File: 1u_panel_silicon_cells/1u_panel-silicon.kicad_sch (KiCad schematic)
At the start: 0 parts

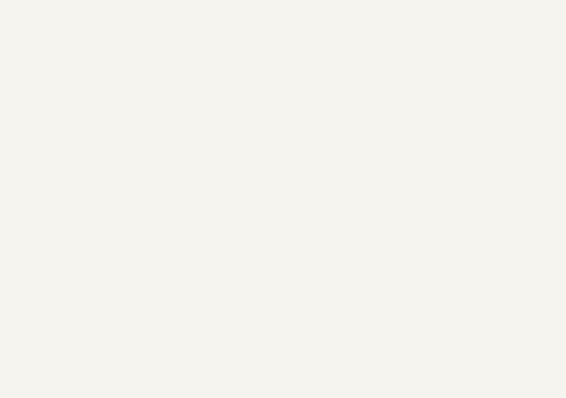
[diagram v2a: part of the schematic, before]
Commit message: Cleanup before fab! Added pullup resistors to ALERTs on TMP101s, removed some paranoia hardware including test points and pullups we don't need, did some schematic polishing for prettiness, and cleaned up some of the zones onthe layout. Removed the need for any old import or local symbol or footprint libraries. Upgraded to v1.1.
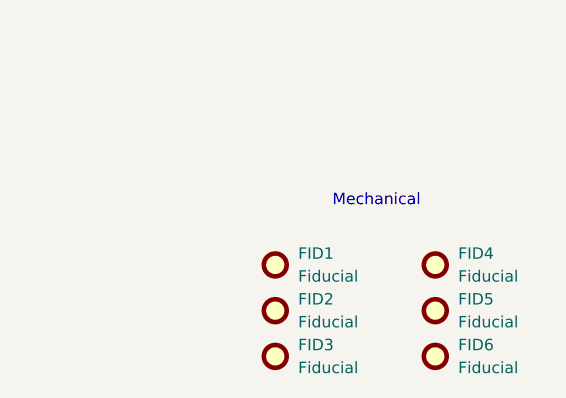
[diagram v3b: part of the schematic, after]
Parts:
- added FID1, FID2, FID3, FID4, FID5, FID6: Fiducial, Fiducial:Fiducial_1mm_Mask2mm, symbol Mechanical:Fiducial
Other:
- note added: "Mechanical"
